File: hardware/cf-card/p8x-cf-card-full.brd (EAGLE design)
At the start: 160 x 100 mm, 27 parts, among them J1 FABC96R, J2 IDE-40, U1 74HCT245, U2 74HCT30, U3 74HCT138, U4 74HCT138, U5 74HCT14, U6 74HCT10, U7 74HCT10, U8 74HCT08, U9 74HCT374

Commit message: feat(hardware): use con-vg DIN 41612 footprints (MABC96R card / FABC96S backplane)
Replace the hand-rolled DIN96/DIN96C connector packages with the real Eagle
con-vg DIN 41612 footprints (geometry baked into the generator so it stays
self-contained): card edge = MABC96R (male right-angle), backplane = FABC96S
(female vertical) — both A/B/C @ 2.54mm, drill 0.9144, two M2.5 mounting holes
at y=+/-45. Card value -> MABC96R; pin->pad names unchanged (A1..C32) so the
netlist is intact.

con-vg centres the pad field on the element origin, so the backplane (hand-
placed/routed) was re-derived: slots dropped to y=54.6 to centre the pin field
on the 109mm board (pads now on-board), bus traces re-routed to the new A/B/C
columns (element at sx(i)-2.54). Cards auto-adapt via fp_box. All 8 boards
validate (0 errors).

Known: 3 placement-overlap WARNINGS on the backplane (power-LED resistor; CT2/RT1
clock terminators, both DNP) where the taller connector crowds the top/bottom
strips — to clear during the Fusion placement pass.

Co-Authored-By: Claude Opus 4.8 <noreply@anthropic.com>
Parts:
- J1: value FABC96R -> MABC96R; device p8x:DIN96C -> p8x:MABC96R
- moved J1 37.5 mm to (7.94, 49.6)

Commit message: feat(hardware): 100nF bypass caps to 0.1" lead pitch on all boards
The 100nF ceramic-disc decoupling/bypass caps used the shared C_DISC footprint
at 0.2" (5.08mm) lead spacing. The parts being sourced are 0.1" (2.54mm) pitch,
so retarget just those caps:

- Add a C_DISC1 footprint (pad 2 at y=-2.54) and a CAP1 device that reuses the
  CAP schematic symbol art but points at C_DISC1.
- Route the 100nF parts to CAP1: per-IC decoupling (CDn), the placement-flow
  copies, and the backplane per-slot caps C1-C10.
- Leave C_DISC (0.2") for the parts that still use it: the 1uF caps, the 150pF
  clock terminators (CT1/CT2), and the XTAL32 placeholder.

Regenerated all 8 boards (.sch/.brd/-full.brd) and the schematic PDFs; the
narrower pad field also relieves the backplane connector clearance. Validation:
0 errors on all boards.

Co-Authored-By: Claude Opus 4.8 <noreply@anthropic.com>
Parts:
- CD1, CD2, CD3, CD4, CD5, CD6, CD7, CD8, CD9: device p8x:C_DISC -> p8x:C_DISC1
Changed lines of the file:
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@@
 <attribute name="VALUE" x="17.87" y="92.66" size="1.778" layer="27" ratio="10"/>
 </element>
-<element name="CD1" library="p8x" package="C_DISC" value="100N" x="29.79" y="95.10" smashed="yes">
+<element name="CD1" library="p8x" package="C_DISC1" value="100N" x="29.79" y="95.10" smashed="yes">
 <attribute name="NAME" x="29.79" y="97.64" size="1.778" layer="25" ratio="10"/>
 <attribute name="VALUE" x="29.79" y="92.56" size="1.778" layer="27" ratio="10"/>
@@
 <attribute name="VALUE" x="34.09" y="92.66" size="1.778" layer="27" ratio="10"/>
 </element>
-<element name="CD2" library="p8x" package="C_DISC" value="100N" x="46.01" y="95.10" smashed="yes">
+<element name="CD2" library="p8x" package="C_DISC1" value="100N" x="46.01" y="95.10" smashed="yes">
 <attribute name="NAME" x="46.01" y="97.64" size="1.778" layer="25" ratio="10"/>
 <attribute name="VALUE" x="46.01" y="92.56" size="1.778" layer="27" ratio="10"/>
@@
 <attribute name="VALUE" x="50.31" y="92.66" size="1.778" layer="27" ratio="10"/>
 </element>
-<element name="CD3" library="p8x" package="C_DISC" value="100N" x="62.23" y="95.10" smashed="yes">
+<element name="CD3" library="p8x" package="C_DISC1" value="100N" x="62.23" y="95.10" smashed="yes">
 <attribute name="NAME" x="62.23" y="97.64" size="1.778" layer="25" ratio="10"/>
 <attribute name="VALUE" x="62.23" y="92.56" size="1.778" layer="27" ratio="10"/>
@@
 <attribute name="VALUE" x="66.53" y="92.66" size="1.778" layer="27" ratio="10"/>
 </element>
-<element name="CD4" library="p8x" package="C_DISC" value="100N" x="78.45" y="95.10" smashed="yes">
+<element name="CD4" library="p8x" package="C_DISC1" value="100N" x="78.45" y="95.10" smashed="yes">
 <attribute name="NAME" x="78.45" y="97.64" size="1.778" layer="25" ratio="10"/>
 <attribute name="VALUE" x="78.45" y="92.56" size="1.778" layer="27" ratio="10"/>
@@
 <attribute name="VALUE" x="82.75" y="92.66" size="1.778" layer="27" ratio="10"/>
 </element>
-<element name="CD5" library="p8x" package="C_DISC" value="100N" x="94.67" y="95.10" smashed="yes">
+<element name="CD5" library="p8x" package="C_DISC1" value="100N" x="94.67" y="95.10" smashed="yes">
 <attribute name="NAME" x="94.67" y="97.64" size="1.778" layer="25" ratio="10"/>
 <attribute name="VALUE" x="94.67" y="92.56" size="1.778" layer="27" ratio="10"/>
@@
 <attribute name="VALUE" x="98.97" y="92.66" size="1.778" layer="27" ratio="10"/>
 </element>
-<element name="CD6" library="p8x" package="C_DISC" value="100N" x="110.89" y="95.10" smashed="yes">
+<element name="CD6" library="p8x" package="C_DISC1" value="100N" x="110.89" y="95.10" smashed="yes">
 <attribute name="NAME" x="110.89" y="97.64" size="1.778" layer="25" ratio="10"/>
 <attribute name="VALUE" x="110.89" y="92.56" size="1.778" layer="27" ratio="10"/>
@@
 <attribute name="VALUE" x="115.19" y="92.66" size="1.778" layer="27" ratio="10"/>
 </element>
-<element name="CD7" library="p8x" package="C_DISC" value="100N" x="127.11" y="95.10" smashed="yes">
+<element name="CD7" library="p8x" package="C_DISC1" value="100N" x="127.11" y="95.10" smashed="yes">
 <attribute name="NAME" x="127.11" y="97.64" size="1.778" layer="25" ratio="10"/>
 <attribute name="VALUE" x="127.11" y="92.56" size="1.778" layer="27" ratio="10"/>
@@
 <attribute name="VALUE" x="131.41" y="92.66" size="1.778" layer="27" ratio="10"/>
 </element>
-<element name="CD8" library="p8x" package="C_DISC" value="100N" x="143.33" y="95.10" smashed="yes">
+<element name="CD8" library="p8x" package="C_DISC1" value="100N" x="143.33" y="95.10" smashed="yes">
 <attribute name="NAME" x="143.33" y="97.64" size="1.778" layer="25" ratio="10"/>
 <attribute name="VALUE" x="143.33" y="92.56" size="1.778" layer="27" ratio="10"/>
@@
 <attribute name="VALUE" x="17.87" y="65.60" size="1.778" layer="27" ratio="10"/>
 </element>
-<element name="CD9" library="p8x" package="C_DISC" value="100N" x="29.79" y="68.04" smashed="yes">
+<element name="CD9" library="p8x" package="C_DISC1" value="100N" x="29.79" y="68.04" smashed="yes">
 <attribute name="NAME" x="29.79" y="70.58" size="1.778" layer="25" ratio="10"/>
 <attribute name="VALUE" x="29.79" y="65.50" size="1.778" layer="27" ratio="10"/>

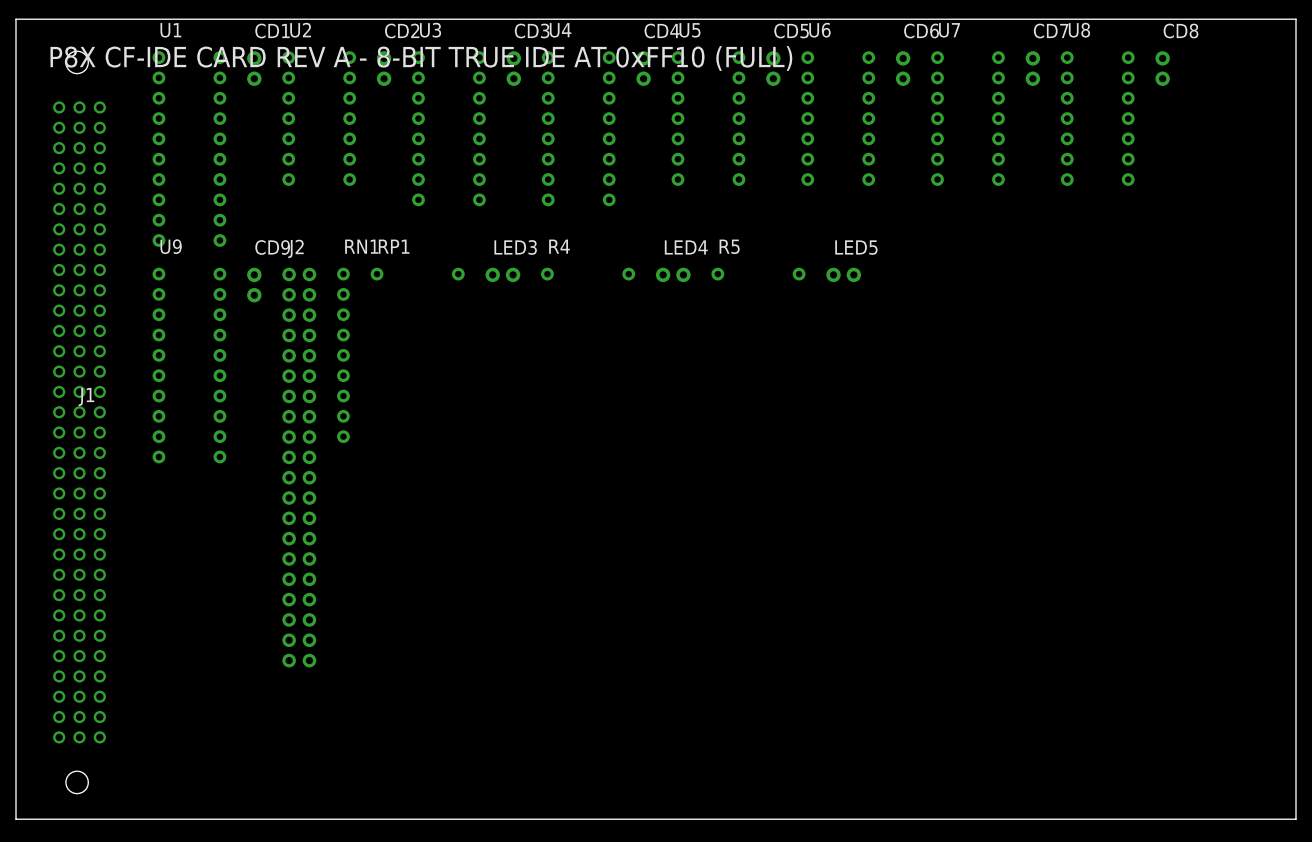
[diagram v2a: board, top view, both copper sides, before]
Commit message: hardware: silkscreen off footprints, standard cap value format, backplane RL1->R1
Pre-Fusion cleanup so there is less to fix by hand once placing/routing.

1. SILKSCREEN NO LONGER OVERLAYS FOOTPRINTS (all boards). NAME/VALUE were emitted
   at the element origin +/-2.54 regardless of part size, so on anything bigger
   than a 2-pin part the text landed ON the pads -- the 96-pin DIN connector had
   J1/SLOT1 across its pad field, and caps had their values on top of them. Now
   placed against the real footprint bbox (fp_box): NAME 0.7mm above the top edge,
   VALUE 0.7mm below the bottom, left-aligned to the box. Verified: 1642
   silkscreen labels across all 9 boards, 0 sitting on a footprint (was many).
   Not rotation-aware, which is fine -- no board rotates a part today.

2. CAPACITOR VALUES use standard unit suffixes: 100N->100nF, 470U->470uF,
   150P->150pF, 1U->1uF (and the DNP/x10 variants). Applied everywhere, so the
   per-IC decoupling caps on every card change too. No doc quoted the raw value
   strings, so no doc churn.

3. BACKPLANE RL1 -> R1 (standard R designator). Scoped to the backplane section
   only -- the io-card and led-card have their own unrelated RL1 (8x330R networks)
   which are untouched. Backplane theory/design docs updated to match.

Part refs/values are decided in gen_eagle.py: the backplane `small=[...]` list and
each cards `ic`/`sm` dicts.

Co-Authored-By: Claude Opus 4.8 <noreply@anthropic.com>
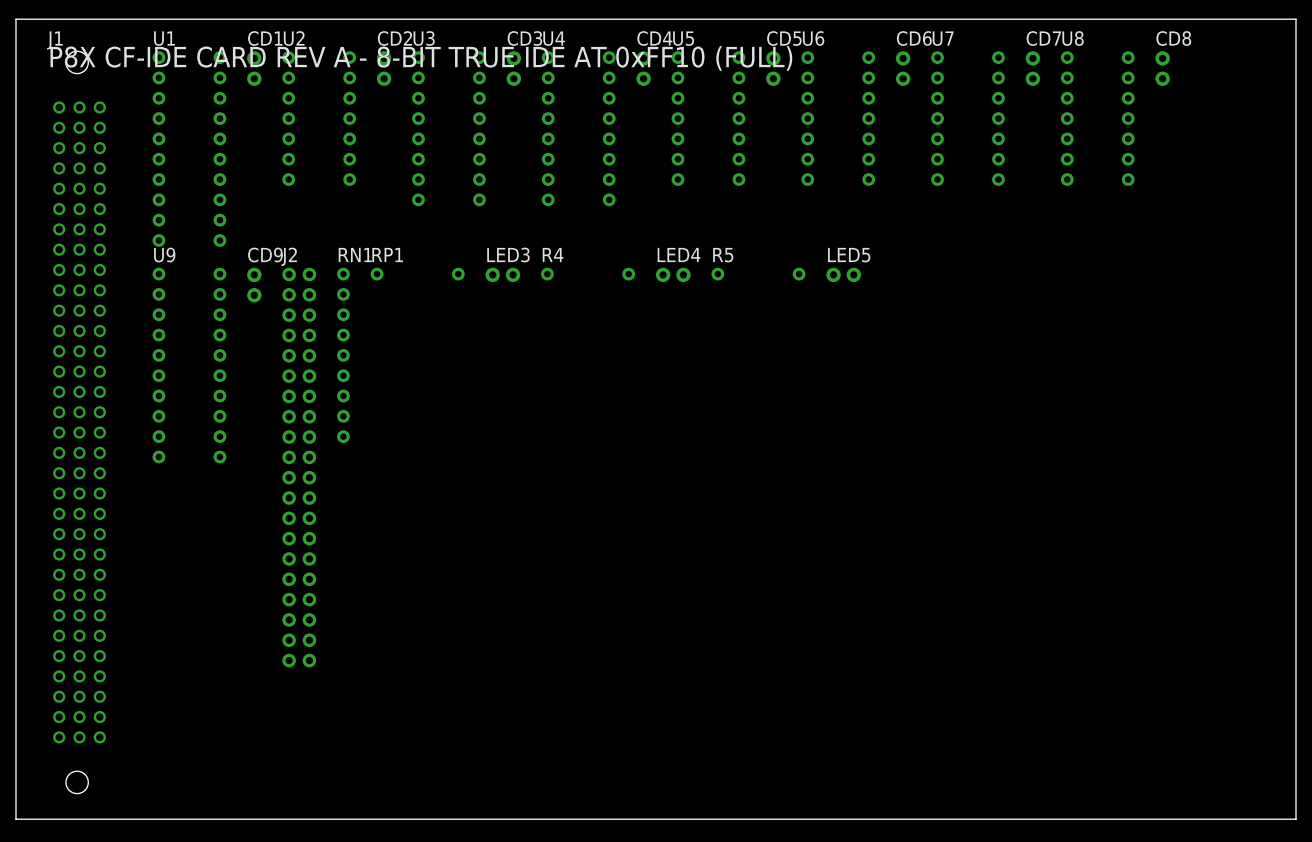
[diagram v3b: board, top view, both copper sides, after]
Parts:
- CD1, CD2, CD3, CD4, CD5, CD6, CD7, CD8, CD9: value 100N -> 100nF
